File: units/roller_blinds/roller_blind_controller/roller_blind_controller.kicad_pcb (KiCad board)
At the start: 2 copper layers, 24.5 x 49.4 mm, 4 parts, among them J1 Conn_01x05, U3 TMC2209_SILENTSTEPSTICK

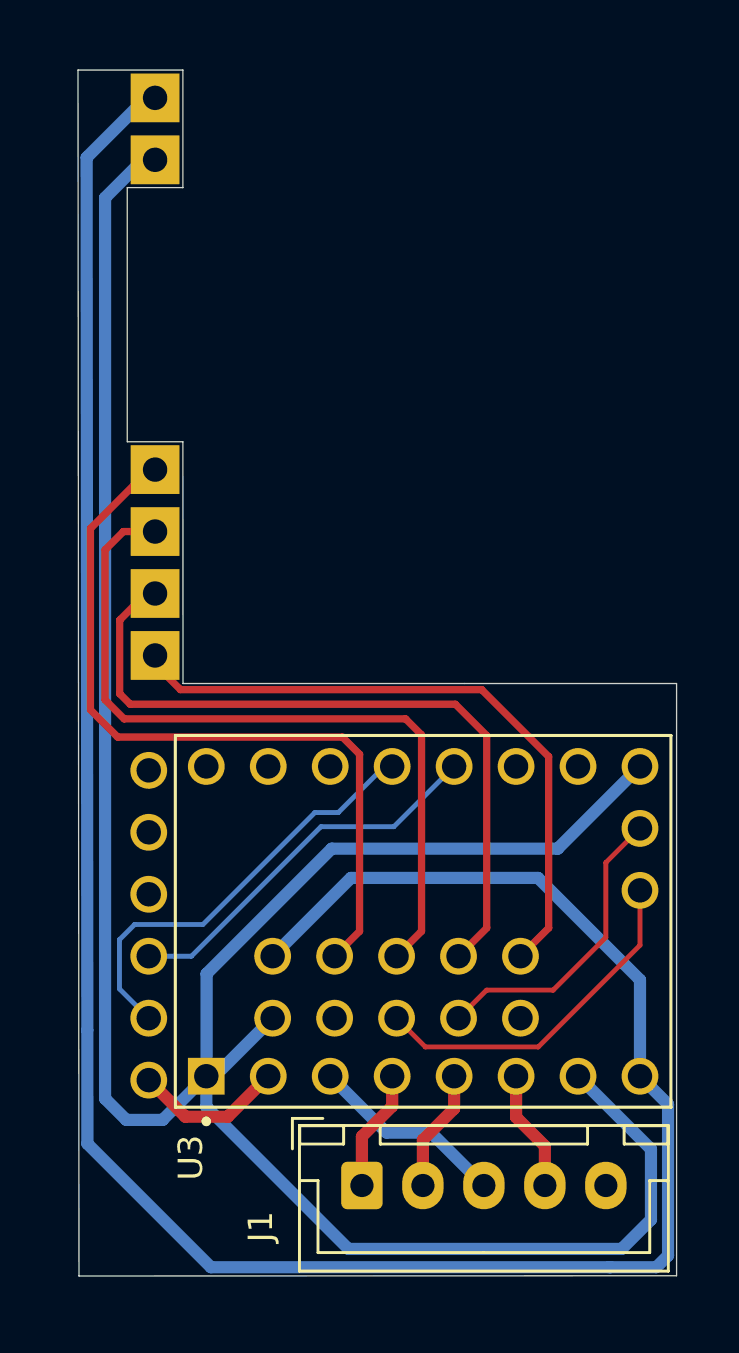
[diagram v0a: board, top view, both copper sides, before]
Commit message: Update units
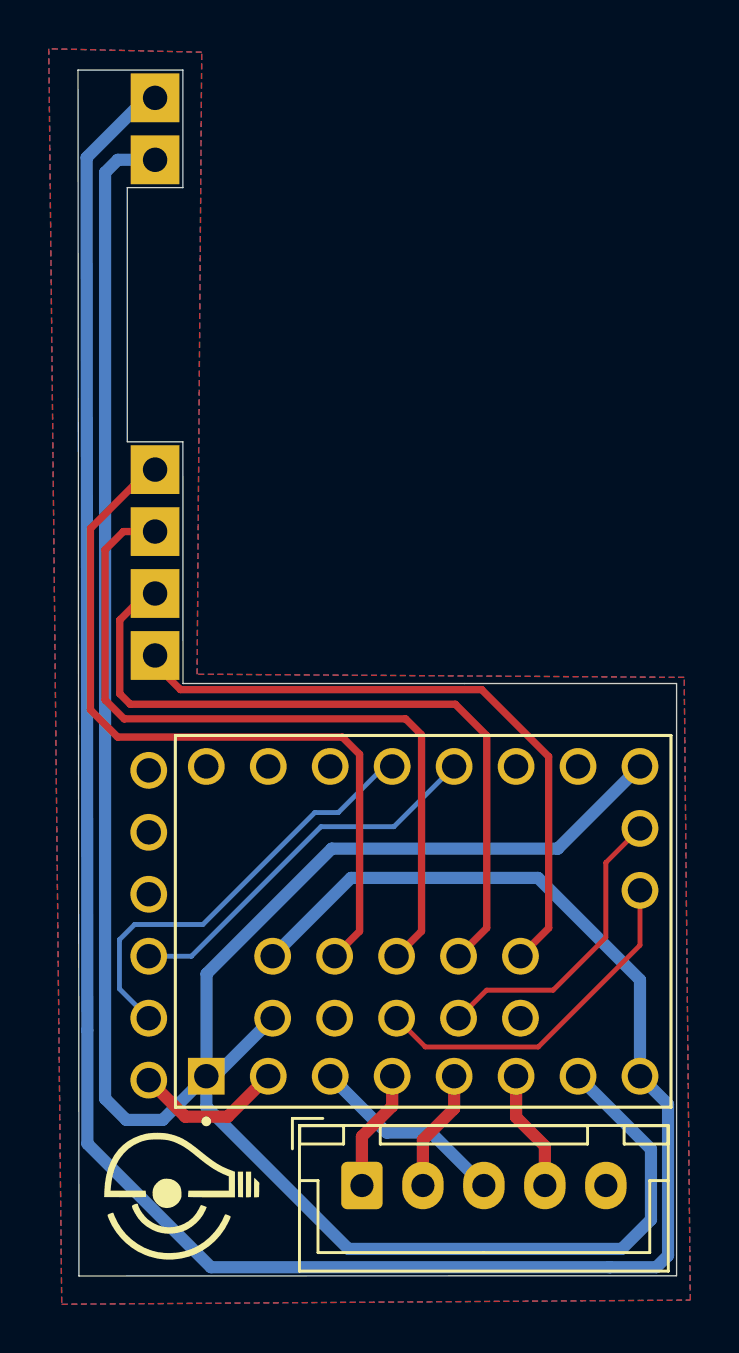
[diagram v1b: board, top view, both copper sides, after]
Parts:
- added G***: LOGO, Logos:Logo, F.Cu at (98.8, 84.0)
- added G***: LOGO, Logos:Logo, B.Cu at (98.8, 83.9)
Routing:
- net GND: track 103.6 -> 104.2 mm
- added copper zone on B.Cu, net GND
- added copper zone on F.Cu, net GND
